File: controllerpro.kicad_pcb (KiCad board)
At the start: 2 copper layers, 80 x 48.3 mm, 24 parts, among them P0 Conn_01x08_Male, P2 Conn_01x08_Male, U1 Teensy3.2

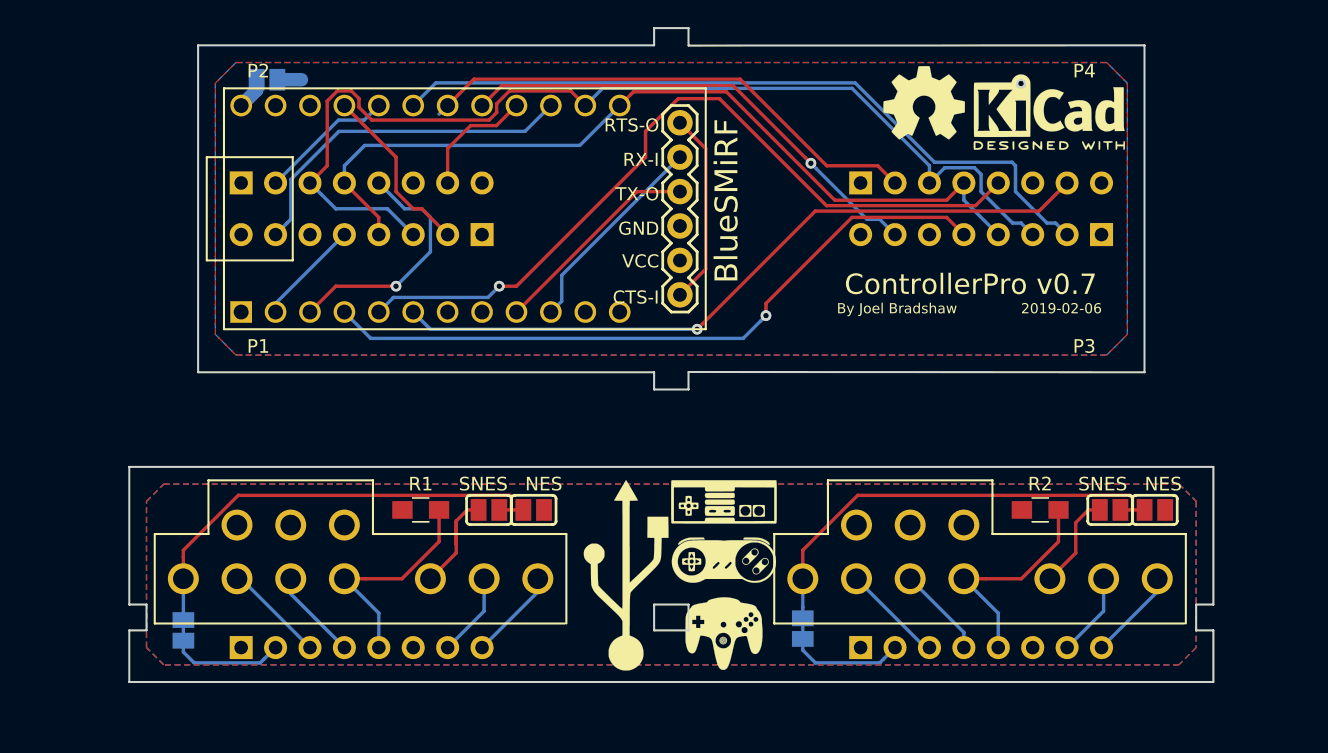
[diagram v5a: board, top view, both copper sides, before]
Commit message: Fixes from hardware debugging
Connect daughterboards to ground (!)
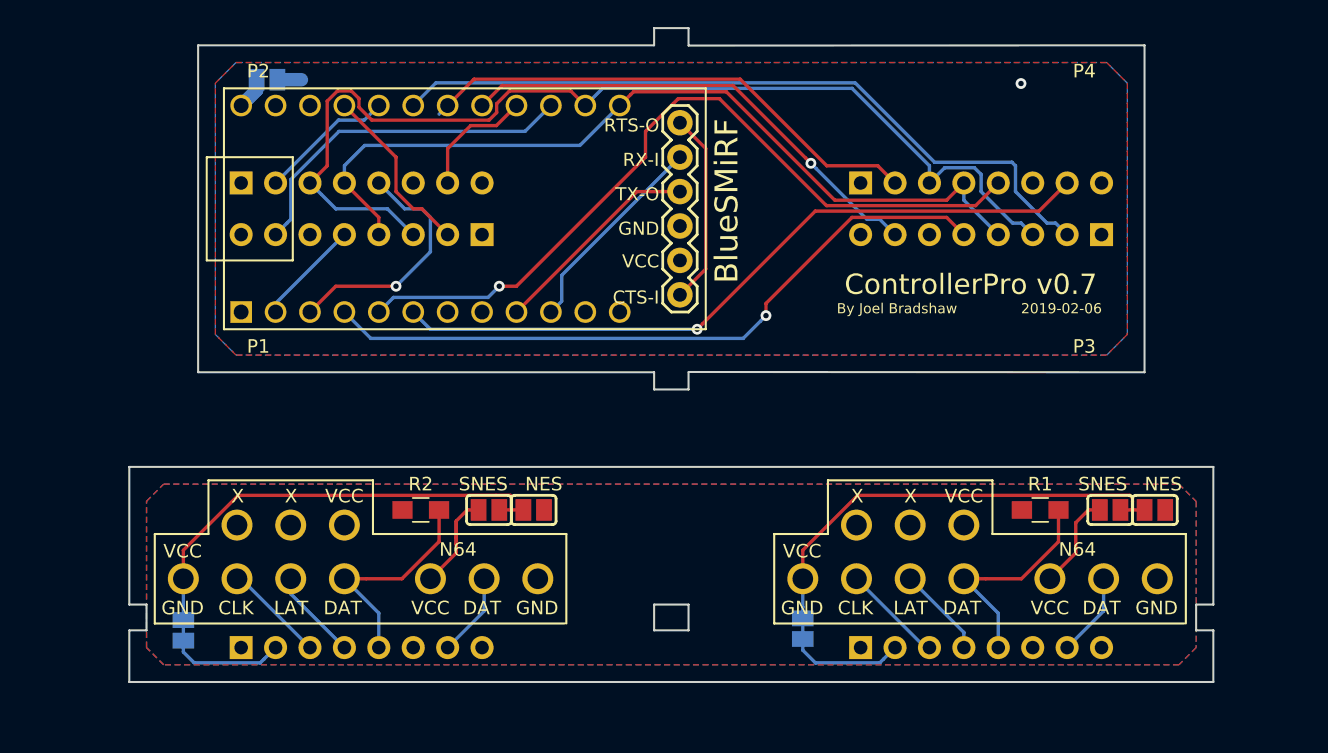
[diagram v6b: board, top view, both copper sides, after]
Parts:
- removed G***: LOGO, logos:square_logo
- removed G***: LOGO, logos:OSHlogo
- removed G***: LOGO, logos:qrcode
- removed G***: LOGO, logos:designedwithkicad
- removed G***: LOGO, logos:sideways
- removed the R1 at (129.5, 127.6)
- added R2: R, Resistors_SMD:R_0805_HandSoldering, F.Cu at (129.5, 127.6)
- renumbered R2 to R1
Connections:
- net Net-(U$1-PadCTS-I) renamed BT_TS
- net Net-(U$1-PadRX-I) renamed BT_RX
- net Net-(U$1-PadTX-0) renamed BT_TX
- P0 pad 8: Net-(P0-Pad8) -> GNDA
- P2 pad 8: Net-(P2-Pad8) -> GNDA
- PORT0 pad 7: Net-(P0-Pad8) -> GNDA
- PORT2 pad 7: Net-(P2-Pad8) -> GNDA
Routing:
- net Net-(P2-Pad8): track 6.78 -> 0.00 mm
- net Net-(P0-Pad8): track 6.78 -> 0.00 mm

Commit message: Split LATCH into four
Also fix misplaced NES VCC (!!) and ports
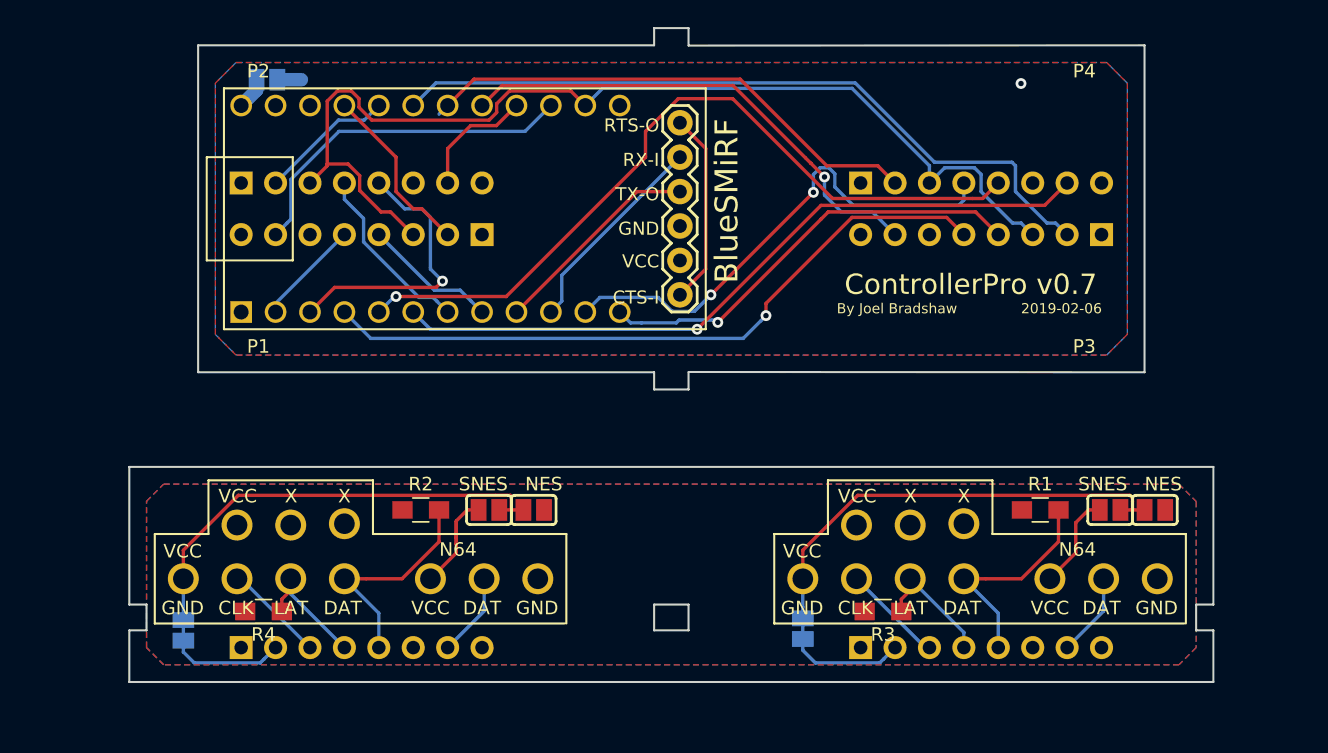
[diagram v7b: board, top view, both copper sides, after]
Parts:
- added R3: R, Resistors_SMD:R_0805_HandSoldering, F.Cu at (163.6, 135.1)
- added R4: R, Resistors_SMD:R_0805_HandSoldering, F.Cu at (117.9, 135.1)
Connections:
- S0 pad 4: LATCH -> LATCH0
- S1 pad 4: LATCH -> LATCH1
- S2 pad 4: LATCH -> LATCH2
- S3 pad 4: LATCH -> LATCH3
- U1 pad 11: Net-(U1-Pad11) -> LATCH1
- U1 pad 12: Net-(U1-Pad12) -> LATCH0
- U1 pad 22: LATCH -> Net-(U1-Pad22)
- U1 pad 7: Net-(U1-Pad7) -> LATCH3
- U1 pad 8: Net-(U1-Pad8) -> LATCH2
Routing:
- net LATCH: track 62.8 -> 0.00 mm
- net LATCH1: track 0.00 -> 37.2 mm, vias 0 -> 2
- net LATCH0: track 0.00 -> 32.5 mm, vias 0 -> 1
- net LATCH3: track 0.00 -> 13.3 mm
- net LATCH2: track 0.00 -> 9.99 mm
- net Net-(P0-Pad4): track 7.20 -> 9.89 mm
- net Net-(P2-Pad4): track 6.72 -> 9.41 mm
- net 5VDATA3: track 18.1 -> 20.7 mm
- net 3VDATA0: track 35.7 -> 36.4 mm
- net 5VDATA1: track 57.3 -> 56.7 mm

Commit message: Make power traces thicker
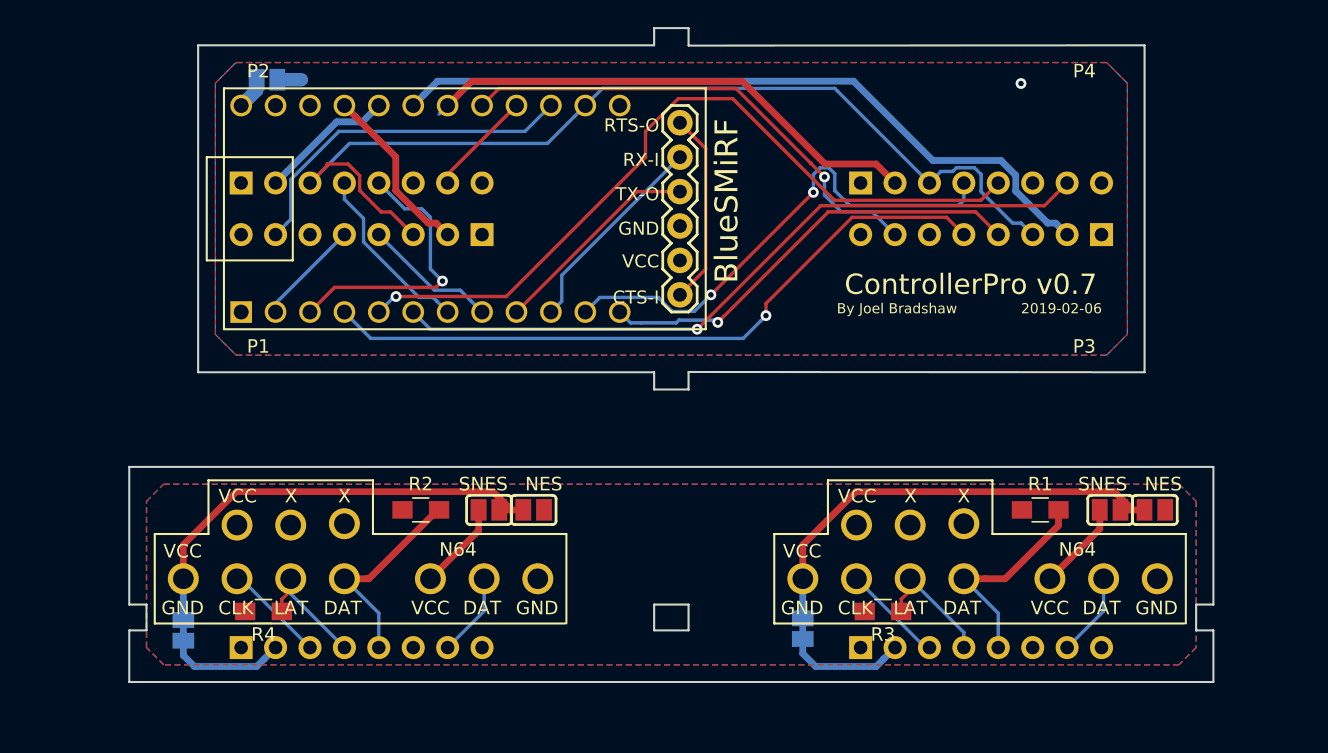
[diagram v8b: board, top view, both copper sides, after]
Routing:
- net CLOCK: track 78.5 -> 73.5 mm
- net VCCA: track 15.8 -> 13.2 mm
- net Net-(JP2-Pad1): track 43.8 -> 45.9 mm
- net 3VDATA3: track 9.57 -> 7.82 mm
- net Net-(P2-Pad5): track 16.6 -> 15.2 mm
- net Net-(P0-Pad5): track 16.6 -> 15.9 mm
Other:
- net class Power added: clearance 0.1524, trace_width 0.5, via_dia 1.6, via_drill 0.8
